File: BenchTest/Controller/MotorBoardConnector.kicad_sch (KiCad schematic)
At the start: 3 parts, among them J8 Conn_01x10

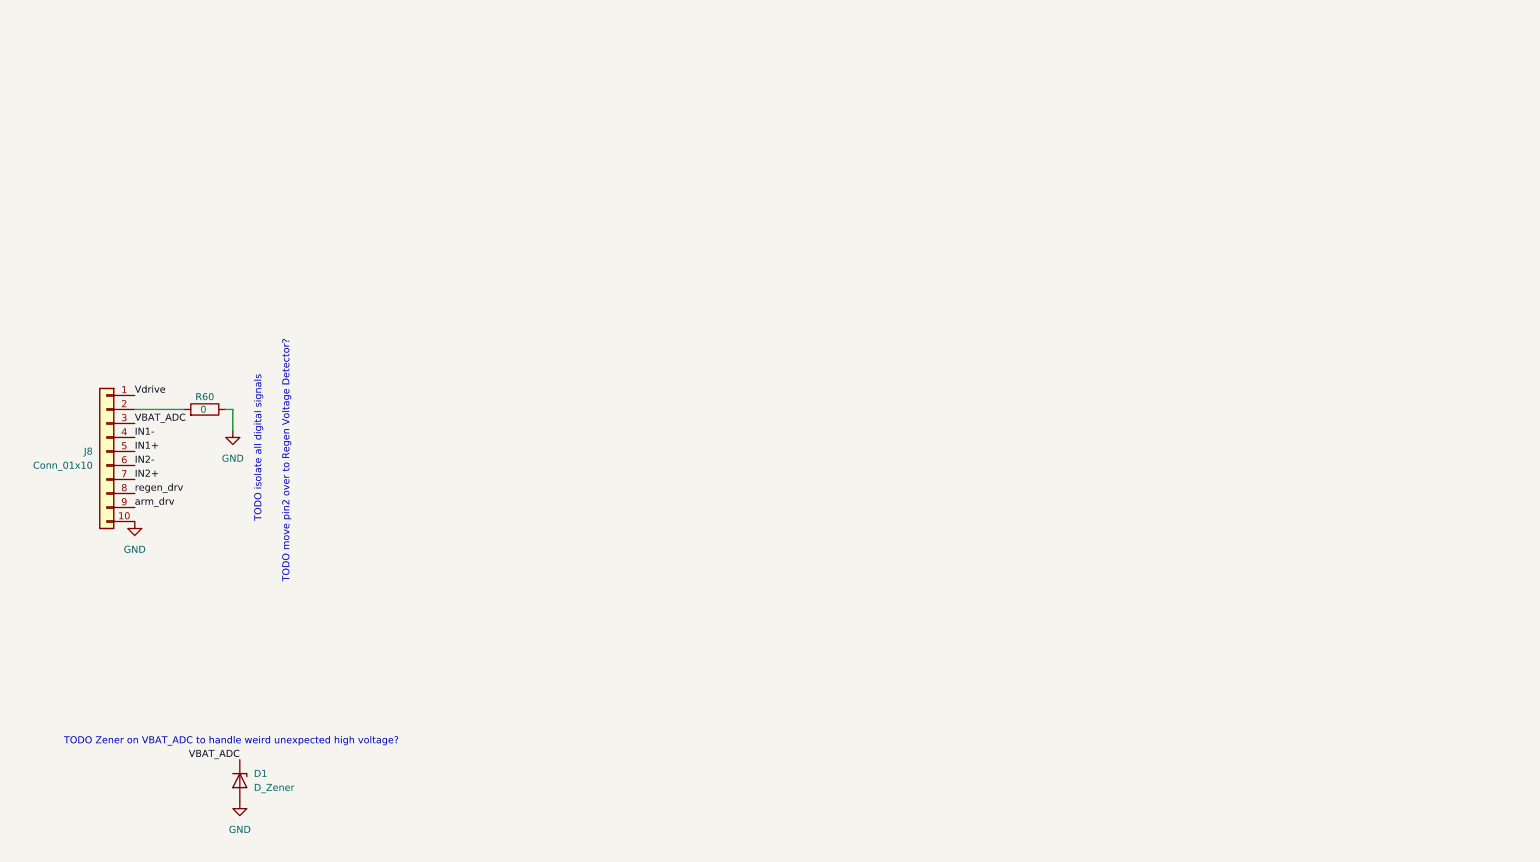
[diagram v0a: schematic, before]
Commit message: Added Isolation for digital drives
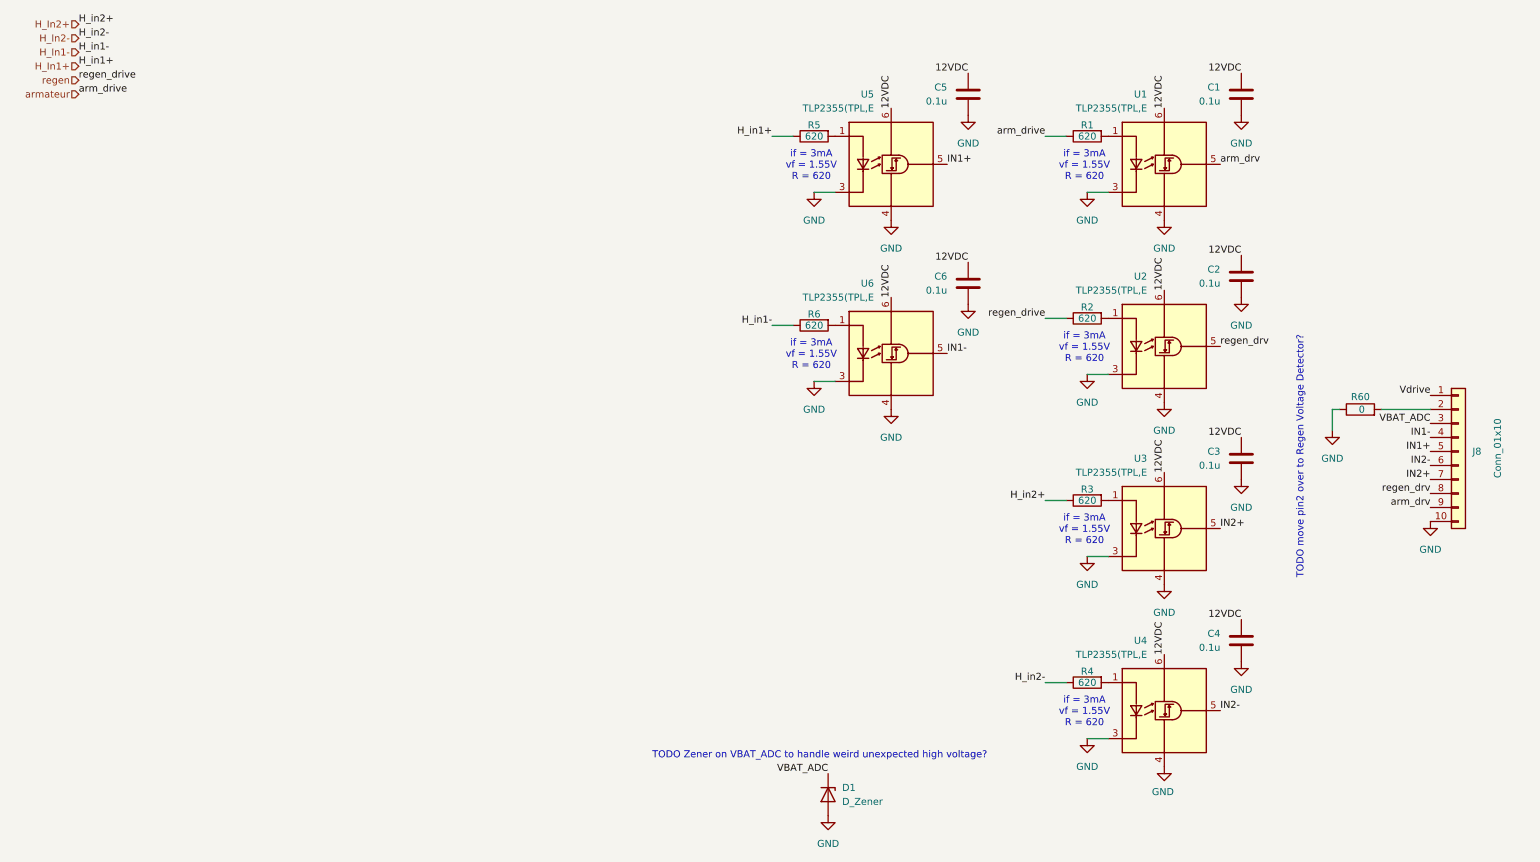
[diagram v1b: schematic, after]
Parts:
- added C1, C2, C3, C4, C5, C6: 0.1u, Capacitor_SMD:C_0402_1005Metric_Pad0.74x0.62mm_HandSolder, symbol Device:C
- added R1, R2, R3, R4, R5, R6: 620, Resistor_SMD:R_0402_1005Metric_Pad0.72x0.64mm_HandSolder, symbol Device:R
- added U1, U2, U3, U4, U5, U6: TLP2355(TPL,E, Package_SO:SO-5-6_4.55x3.7mm_P1.27mm, symbol Isolator:TLP2310
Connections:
- net GND: now also C1.2, C2.2, C3.2, C4.2, C5.2, C6.2, U1.3 (K), U1.4 (GND), U2.3 (K), U2.4 (GND), U3.3 (K), U3.4 (GND), U4.3 (K), U4.4 (GND), U5.3 (K), U5.4 (GND), U6.3 (K), U6.4 (GND)
- net IN1+: now also U5.5 (VO)
- net IN1-: now also U6.5 (VO)
- net IN2+: now also U3.5 (VO)
- net IN2-: now also U4.5 (VO)
- net arm_drv: now also U1.5 (VO)
- net regen_drv: now also U2.5 (VO)
- new net: R3.2, U3.1 (A)
- new net: R2.2, U2.1 (A)
- new net: R1.2, U1.1 (A)
- new net: R5.2, U5.1 (A)
- new net: R6.2, U6.1 (A)
- new net: R4.2, U4.1 (A)
- new net 12VDC: C1.1, C2.1, C3.1, C4.1, C5.1, C6.1, U1.6 (VDD), U2.6 (VDD), U3.6 (VDD), U4.6 (VDD), U5.6 (VDD), U6.6 (VDD)
- new net H_In1+: R5.1
- new net H_In1-: R6.1
- new net H_In2+: R3.1
- new net H_In2-: R4.1
- new net armateur: R1.1
- new net regen: R2.1
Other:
- note added: "if = 3mA vf = 1.55V R = 620"
- note removed: "TODO isolate all digital signals"
- moved on the sheet: D1, J8, R60

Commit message: Added VMOT Measurements
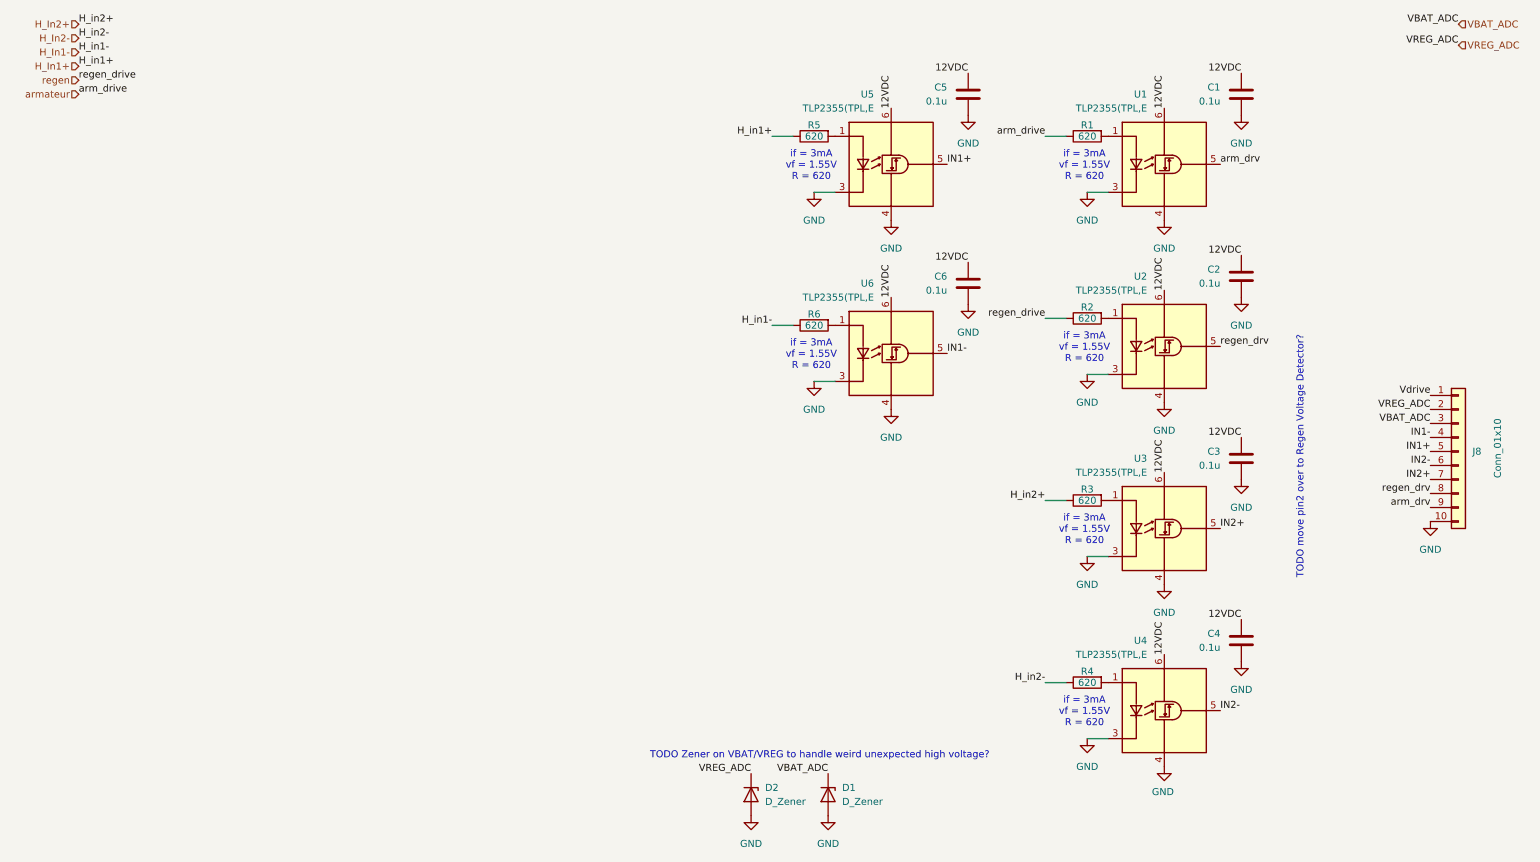
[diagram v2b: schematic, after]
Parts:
- removed R60: 0, symbol Device:R
- added D2: D_Zener, symbol Device:D_Zener
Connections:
- net GND: now also D2.2 (A)
- net VREG_ADC: now reaches J8.2 (Pin_2)
- net VREG_ADC: now also D2.1 (K)
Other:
- note added: "TODO Zener on VBAT/VREG to handle weird unexpected high voltage?"
- note removed: "TODO Zener on VBAT_ADC to handle weird unexpected high voltage?"
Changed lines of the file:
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@@
 		)
 	)
-	(text "TODO Zener on VBAT_ADC to handle weird unexpected high voltage?"
+	(text "TODO Zener on VBAT/VREG to handle weird unexpected high voltage?"
 		(exclude_from_sim no)
 		(at 157.226 147.828 0)
@@
 	(wire
 		(pts
-			(xy 250.19 88.9) (xy 250.19 85.09)
+			(xy 209.55 111.76) (xy 205.74 111.76)
 		)
 		(stroke
@@
 	(wire
 		(pts
-			(xy 209.55 111.76) (xy 205.74 111.76)
+			(xy 160.02 80.01) (xy 156.21 80.01)
 		)
 		(stroke
@@
 	(wire
 		(pts
-			(xy 160.02 80.01) (xy 156.21 80.01)
+			(xy 152.4 69.85) (xy 148.59 69.85)
 		)
 		(stroke
@@
 	(wire
 		(pts
-			(xy 152.4 69.85) (xy 148.59 69.85)
+			(xy 160.02 45.72) (xy 156.21 45.72)
 		)
 		(stroke
@@
 	(wire
 		(pts
-			(xy 160.02 45.72) (xy 156.21 45.72)
+			(xy 209.55 144.78) (xy 205.74 144.78)
 		)
 		(stroke
@@
 	(wire
 		(pts
-			(xy 209.55 144.78) (xy 205.74 144.78)
+			(xy 201.93 68.58) (xy 198.12 68.58)
 		)
 		(stroke
@@
 	(wire
 		(pts
-			(xy 201.93 68.58) (xy 198.12 68.58)
+			(xy 201.93 101.6) (xy 198.12 101.6)
 		)
 		(stroke
@@
 	(wire
 		(pts
-			(xy 250.19 85.09) (xy 251.46 85.09)
+			(xy 201.93 134.62) (xy 198.12 134.62)
 		)
 		(stroke
@@
 	(wire
 		(pts
-			(xy 201.93 101.6) (xy 198.12 101.6)
+			(xy 152.4 35.56) (xy 148.59 35.56)
 		)
 		(stroke
@@
 	(wire
 		(pts
-			(xy 259.08 85.09) (xy 267.97 85.09)
+			(xy 209.55 78.74) (xy 205.74 78.74)
 		)
 		(stroke
@@
 	(wire
 		(pts
-			(xy 201.93 134.62) (xy 198.12 134.62)
+			(xy 201.93 35.56) (xy 198.12 35.56)
 		)
 		(stroke
@@
 		)
 	)
-	(wire
-		(pts
-			(xy 152.4 35.56) (xy 148.59 35.56)
-		)
-		(stroke
-			(width 0)
-			(type default)
-		)
-	)
-	(wire
-		(pts
-			(xy 209.55 78.74) (xy 205.74 78.74)
-		)
-		(stroke
-			(width 0)
-			(type default)
-		)
-	)
-	(wire
-		(pts
-			(xy 201.93 35.56) (xy 198.12 35.56)
-		)
-		(stroke
-			(width 0)
-			(type default)
-		)
-	)
 	(label "H_in1-"
 		(at 22.86 20.32 0)
@@
 		)
 	)
+	(label "VREG_ADC"
+		(at 267.97 85.09 180)
+		(effects
+			(font
+				(size 1.27 1.27)
+			)
+			(justify right bottom)
+		)
+	)
 	(label "IN1+"
 		(at 180.34 40.64 0)
@@
 		)
 	)
+	(label "VREG_ADC"
+		(at 273.05 19.05 180)
+		(effects
+			(font
+				(size 1.27 1.27)
+			)
+			(justify right bottom)
+		)
+	)
 	(label "IN1-"
 		(at 267.97 90.17 180)
@@
 		)
 	)
+	(label "VBAT_ADC"
+		(at 273.05 15.24 180)
+		(effects
+			(font
+				(size 1.27 1.27)
+			)
+			(justify right bottom)
+		)
+	)
 	(label "IN2-"
 		(at 267.97 95.25 180)
@@
 			)
 			(justify left bottom)
+		)
+	)
+	(label "VREG_ADC"
+		(at 144.78 151.13 180)
+		(effects
+			(font
+				(size 1.27 1.27)
+			)
+			(justify right bottom)
 		)
 	)
@@
 		)
 	)
+	(hierarchical_label "VBAT_ADC"
+		(shape input)
+		(at 273.05 15.24 0)
+		(effects
+			(font
+				(size 1.27 1.27)
+			)
+			(justify left)
+		)
+	)
+	(hierarchical_label "VREG_ADC"
+		(shape input)
+		(at 273.05 19.05 0)
+		(effects
+			(font
+				(size 1.27 1.27)
+			)
+			(justify left)
+		)
+	)
 	(hierarchical_label "H_In2-"
 		(shape input)
@@
 	)
 	(symbol
-		(lib_id "Device:R")
-		(at 255.27 85.09 90)
-		(unit 1)
-		(exclude_from_sim no)
-		(in_bom yes)
-		(on_board yes)
-		(dnp no)
-		(property "Reference" "R60"
-			(at 255.27 82.804 90)
-			(effects
-				(font
-					(size 1.27 1.27)
-				)
-			)
-		)
-		(property "Value" "0"
-			(at 255.524 85.09 90)
-			(effects
-				(font
-					(size 1.27 1.27)
-				)
+		(lib_id "Device:D_Zener")
+		(at 144.78 154.94 270)
+		(unit 1)
+		(exclude_from_sim no)
+		(in_bom yes)
+		(on_board yes)
+		(dnp no)
+		(fields_autoplaced yes)
+		(property "Reference" "D2"
+			(at 147.32 153.6699 90)
+			(effects
+				(font
+					(size 1.27 1.27)
+				)
+				(justify left)
+			)
+		)
+		(property "Value" "D_Zener"
+			(at 147.32 156.2099 90)
+			(effects
+				(font
+					(size 1.27 1.27)
+				)
+				(justify left)
 			)
 		)
 		(property "Footprint" ""
-			(at 255.27 86.868 90)
+			(at 144.78 154.94 0)
 			(effects
 				(font
@@
 		)
 		(property "Datasheet" "~"
-			(at 255.27 85.09 0)
-			(effects
-				(font
-					(size 1.27 1.27)
-				)
-				(hide yes)
-			)
-		)
-		(property "Description" "Resistor"
-			(at 255.27 85.09 0)
-			(effects
-				(font
-					(size 1.27 1.27)
-				)
-				(hide yes)
-			)
+			(at 144.78 154.94 0)
+			(effects
+				(font
+					(size 1.27 1.27)
+				)
+				(hide yes)
+			)
+		)
+		(property "Description" "Zener diode"
+			(at 144.78 154.94 0)
+			(effects
+				(font
+					(size 1.27 1.27)
+				)
+				(hide yes)
+			)
+		)
+		(pin "1"
 		)
 		(pin "2"
 		)
-		(pin "1"
-		)
 		(instances
 			(project "Controller"
 				(path "/3d2636da-949a-430f-b429-214c7142e7ac/680043cb-bc9c-44e2-8bc3-261f88bf76fe"
-					(reference "R60")
+					(reference "D2")
 					(unit 1)
 				)
@@
 	)
 	(symbol
-		(lib_id "power:GND")
-		(at 250.19 88.9 0)
-		(unit 1)
-		(exclude_from_sim no)
-		(in_bom yes)
-		(on_board yes)
-		(dnp no)
-		(fields_autoplaced yes)
-		(property "Reference" "#PWR037"
-			(at 250.19 95.25 0)
-			(effects
-				(font
-					(size 1.27 1.27)
-				)
-				(hide yes)
-			)
-		)
-		(property "Value" "GND"
-			(at 250.19 93.98 0)
-			(effects
-				(font
-					(size 1.27 1.27)
-				)
-			)
-		)
-		(property "Footprint" ""
-			(at 250.19 88.9 0)
-			(effects
-				(font
-					(size 1.27 1.27)
-				)
-				(hide yes)
-			)
-		)
-		(property "Datasheet" ""
-			(at 250.19 88.9 0)
-			(effects
-				(font
-					(size 1.27 1.27)
-				)
-				(hide yes)
-			)
-		)
-		(property "Description" "Power symbol creates a global label with name \"GND\" , ground"
-			(at 250.19 88.9 0)
-			(effects
-				(font
-					(size 1.27 1.27)
-				)
-				(hide yes)
-			)
-		)
-		(pin "1"
-		)
-		(instances
-			(project "Controller"
-				(path "/3d2636da-949a-430f-b429-214c7142e7ac/680043cb-bc9c-44e2-8bc3-261f88bf76fe"
-					(reference "#PWR037")
-					(unit 1)
-				)
-			)
-		)
-	)
-	(symbol
 		(lib_id "Device:R")
 		(at 205.74 101.6 90)
@@
 					(unit 1)
 				)
+			)
+		)
+	)
+	(symbol
+		(lib_id "power:GND")
+		(at 144.78 158.75 0)
+		(unit 1)
+		(exclude_from_sim no)
+		(in_bom yes)
+		(on_board yes)
+		(dnp no)
+		(fields_autoplaced yes)
+		(property "Reference" "#PWR023"
+			(at 144.78 165.1 0)
+			(effects
+				(font
+					(size 1.27 1.27)
+				)
+				(hide yes)
+			)
+		)
+		(property "Value" "GND"
+			(at 144.78 163.83 0)
+			(effects
+				(font
+					(size 1.27 1.27)
+				)
+			)
+		)
+		(property "Footprint" ""
+			(at 144.78 158.75 0)
+			(effects
+				(font
+					(size 1.27 1.27)
+				)
+				(hide yes)
+			)
+		)
+		(property "Datasheet" ""
+			(at 144.78 158.75 0)
+			(effects
+				(font
+					(size 1.27 1.27)
+				)
+				(hide yes)
+			)
+		)
+		(property "Description" "Power symbol creates a global label with name \"GND\" , ground"
+			(at 144.78 158.75 0)
+			(effects
+				(font
+					(size 1.27 1.27)
+				)
+				(hide yes)
+			)
+		)
+		(pin "1"
+		)
+		(instances
+			(project "Controller"
+				(path "/3d2636da-949a-430f-b429-214c7142e7ac/680043cb-bc9c-44e2-8bc3-261f88bf76fe"
+					(reference "#PWR023")
+					(unit 1)
+				)

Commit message: WIP Controller in progress
w
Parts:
- D1, D2: footprint (none) -> Diode_SMD:D_SOD-123F
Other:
- note added: "Neither ADC is expected to exceed 3.0V. Zener set to 3.2V breakdown At 3.2V: 200mV above expected dynamic range, but not harmful to electronics"
- note removed: "TODO Zener on VBAT/VREG to handle weird unexpected high voltage?"
- note removed: "TODO move pin2 over to Regen Voltage Detector?"
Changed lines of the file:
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@@
 	(generator_version "9.0")
 	(paper "A4")
-	(text "TODO move pin2 over to Regen Voltage Detector?"
-		(exclude_from_sim no)
-		(at 244.348 93.726 90)
+	(text "Neither ADC is expected to exceed 3.0V.\nZener set to 3.2V breakdown\nAt 3.2V: 200mV above expected dynamic range, but not harmful to electronics"
+		(exclude_from_sim no)
+		(at 147.828 144.018 0)
 		(effects
 			(font
@@
 		(exclude_from_sim no)
 		(at 155.702 40.894 0)
-		(effects
-			(font
-				(size 1.27 1.27)
-			)
-		)
-	)
-	(text "TODO Zener on VBAT/VREG to handle weird unexpected high voltage?"
-		(exclude_from_sim no)
-		(at 157.226 147.828 0)
 		(effects
 			(font
@@
 			)
 		)
-		(property "Footprint" ""
+		(property "Footprint" "Diode_SMD:D_SOD-123F"
 			(at 144.78 154.94 0)
 			(effects
@@
 			)
 		)
-		(property "Description" "Zener diode"
+		(property "Description" "KDZVTR3.0B"
 			(at 144.78 154.94 0)
 			(effects
@@
 			)
 		)
-		(property "Footprint" ""
+		(property "Footprint" "Diode_SMD:D_SOD-123F"
 			(at 158.75 154.94 0)
 			(effects
@@
 			)
 		)
-		(property "Description" "Zener diode"
+		(property "Description" "KDZVTR3.0B"
 			(at 158.75 154.94 0)
 			(effects
